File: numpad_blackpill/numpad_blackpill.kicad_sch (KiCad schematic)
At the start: 51 parts

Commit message: working on numpad PCB
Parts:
- removed U?: STM32F411CEUx, Package_DFN_QFN:QFN-48-1EP_7x7mm_P0.5mm_EP5.6x5.6mm, symbol MCU_ST_STM32F4:STM32F411CEUx
- added U1: YAAJ_BlackPill, Kicad-STM32-master:YAAJ_BlackPill_SWD_1, symbol YAAJ_BlackPill:YAAJ_BlackPill
- SW1, SW10, SW11, SW12, SW13, SW14, SW15, SW16, SW17, SW18, SW19, SW2, SW20, SW21, SW22, SW23, SW24, SW25, SW3, SW4, SW5, SW6, SW7, SW8, SW9: renamed from SW?; footprint (none) -> Button_Switch_Keyboard:SW_Cherry_MX_1.00u_PCB
- gave numbers to parts that had none: 25
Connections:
- net Col1: now also U1.13 (PB5)
- net Col2: now also U1.14 (PB6)
- net Col3: now also U1.15 (PB7)
- net Col4: now also U1.19 (PB8)
- net Col5: now also U1.20 (PB9)
- net Reset: now also U1.22 (RST)
- net Row1: now also U1.24 (PA1)
- net Row2: now also U1.25 (PA2)
- net Row3: now also U1.26 (PA3)
- net Row4: now also U1.27 (PA4)
- net Row5: now also U1.28 (PA5)

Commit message: finished basic numpad with blackpill
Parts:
- removed D1, D15, D22, D24, D6: 1N4148, Diode_THT:D_DO-35_SOD27_P7.62mm_Horizontal, symbol Diode:1N4148
- removed SW1, SW15, SW22, SW24, SW6: SW_Push, Button_Switch_Keyboard:SW_Cherry_MX_1.00u_PCB, symbol Switch:SW_Push
- removed U1: YAAJ_BlackPill, Kicad-STM32-master:YAAJ_BlackPill_SWD_1, symbol YAAJ_BlackPill:YAAJ_BlackPill
- added U1: YAAJ_BlackPill_Part_Like_SWD_Breakout, Kicad-STM32-master:YAAJ_BlackPill_SWD_3, symbol YAAJ_BlackPill_Part_Like_SWD_Breakout:YAAJ_BlackPill_Part_Like_SWD_Breakout
- SW19: renamed from SW23; footprint Button_Switch_Keyboard:SW_Cherry_MX_1.00u_PCB -> Button_Switch_Keyboard:SW_Cherry_MX_2.00u_Vertical_PCB
- SW20: renamed from SW25; footprint Button_Switch_Keyboard:SW_Cherry_MX_1.00u_PCB -> Button_Switch_Keyboard:SW_Cherry_MX_2.00u_Vertical_PCB
- SW8: renamed from SW10; footprint Button_Switch_Keyboard:SW_Cherry_MX_1.00u_PCB -> Button_Switch_Keyboard:SW_Cherry_MX_2.00u_PCB
- renumbered D2 to D1, D12 to D10, D13 to D11, D14 to D12, D16 to D13, D17 to D14, D18 to D15, D19 to D16, D20 to D17, D21 to D18, D23 to D19, D3 to D2, D25 to D20, D4 to D3, D5 to D4, D7 to D5, D8 to D6, D9 to D7, D10 to D8, D11 to D9, SW2 to SW1, SW12 to SW10, SW13 to SW11, SW14 to SW12, SW16 to SW13, SW17 to SW14, SW18 to SW15, SW19 to SW16, SW20 to SW17, SW21 to SW18, SW3 to SW2, SW4 to SW3, SW5 to SW4, SW7 to SW5, SW8 to SW6, SW9 to SW7, SW11 to SW9
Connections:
- net Col1: now also U1.7 (PA10)
- net Col2: now also U1.6 (PA9)
- net Col3: now also U1.13 (PB5)
- net Col4: now also U1.14 (PB6)
- net Col5: now also U1.15 (PB7)
- net Reset: now also U1.22 (RST)
- net Row1: now also U1.28 (PA5)
- net Row2: now also U1.27 (PA4)
- net Row3: now also U1.26 (PA3)
- net Row4: now also U1.25 (PA2)
- net Row5: now also U1.24 (PA1)
- new net GND: U1.17 (GND), U1.18 (GND)
- no-connect marks 0 -> 20

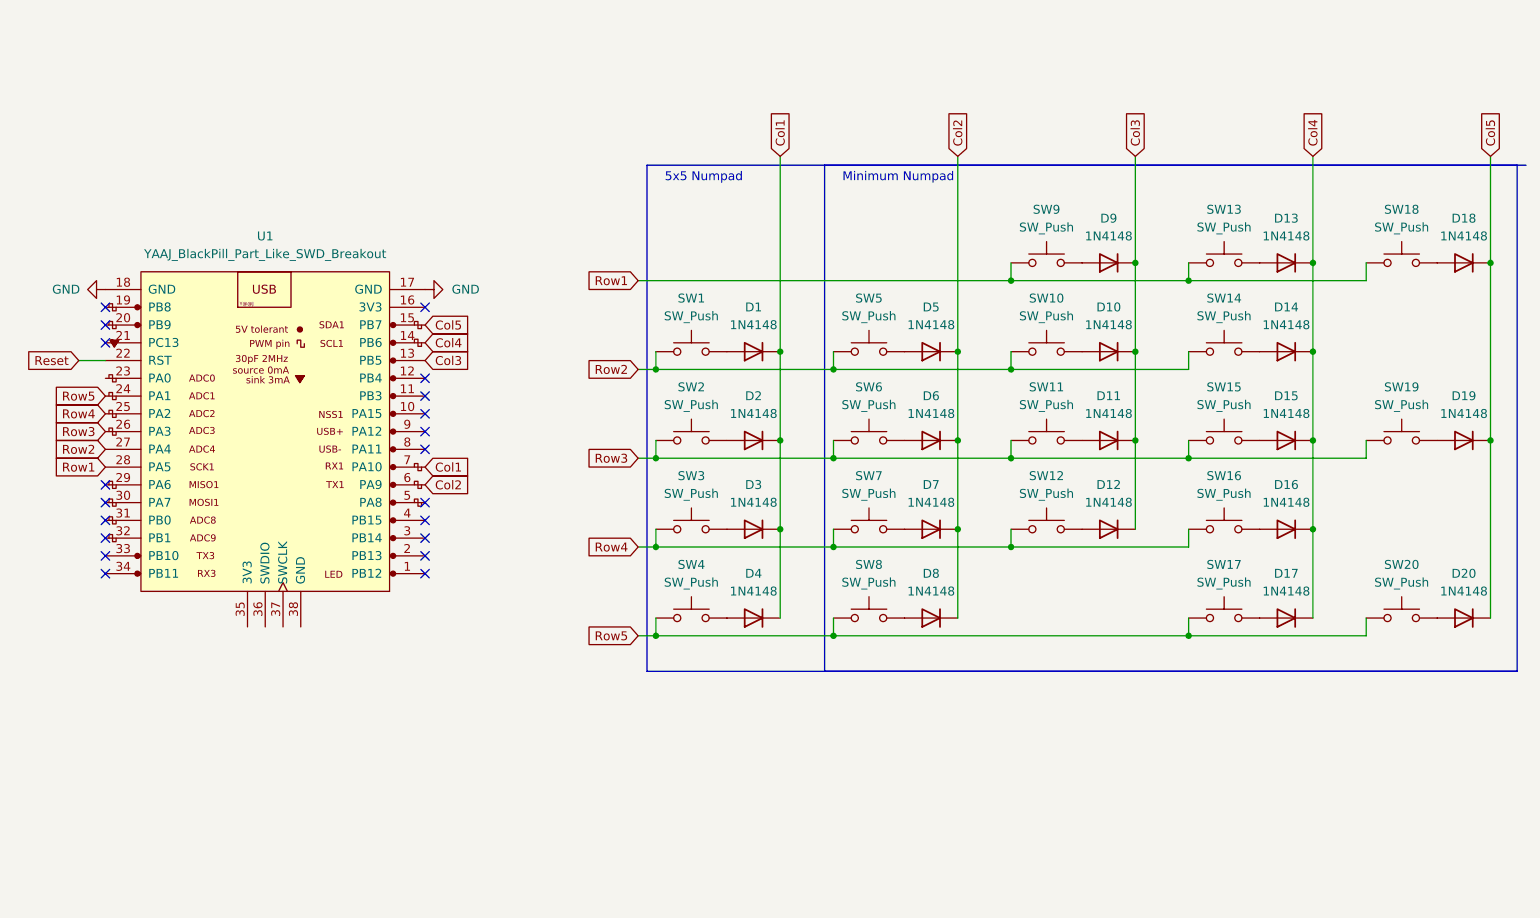
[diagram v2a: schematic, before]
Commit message: removed encoder from numpad
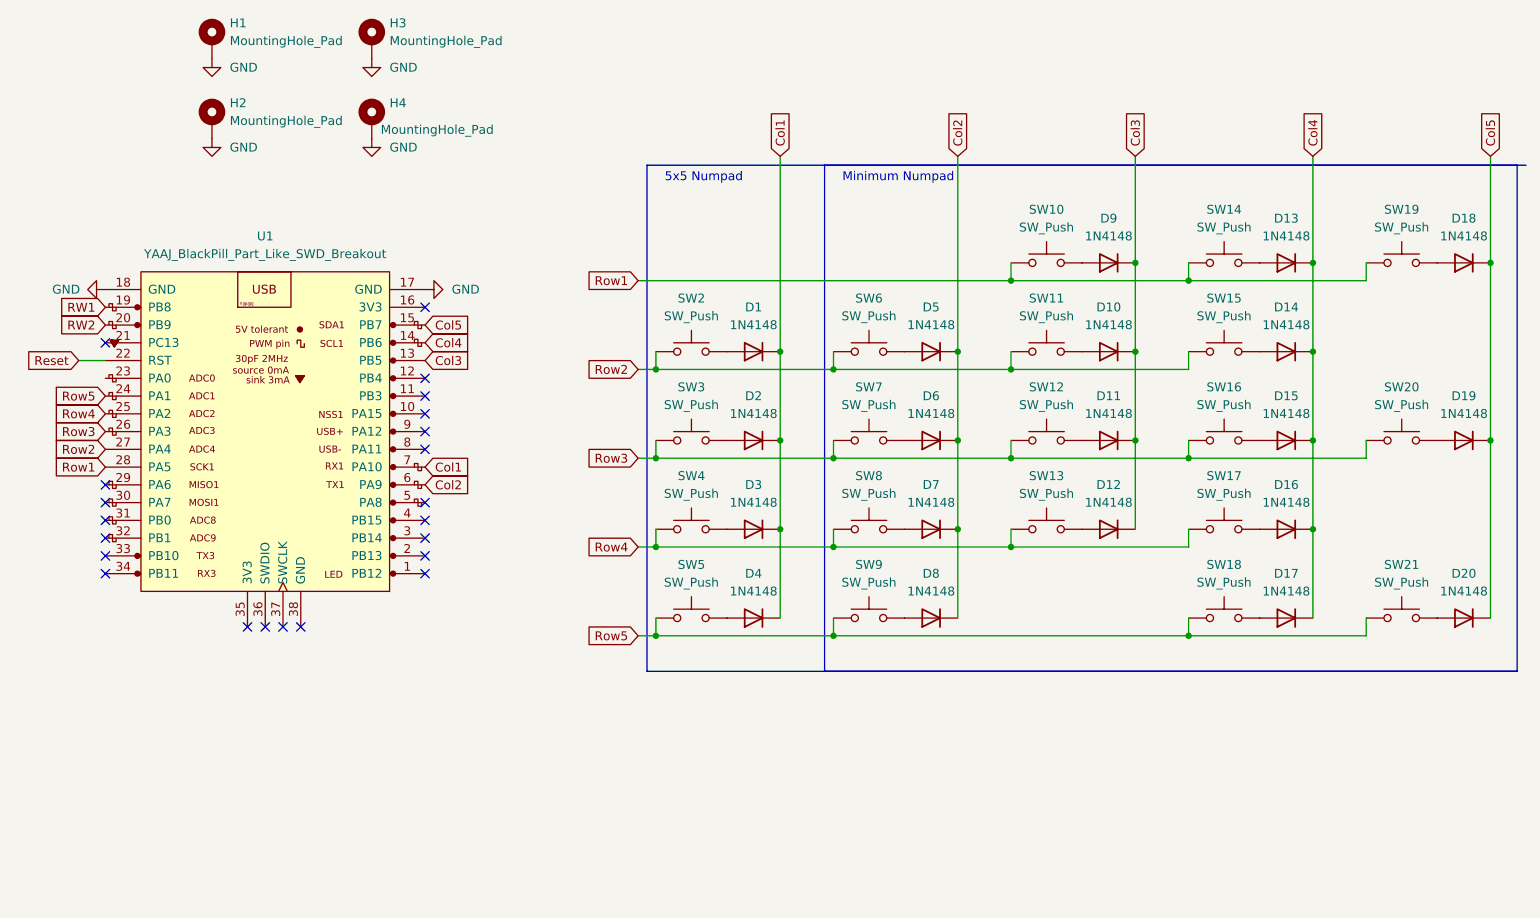
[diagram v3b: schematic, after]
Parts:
- added H1, H2, H3, H4: MountingHole_Pad, MountingHole:MountingHole_2mm, symbol Mechanical:MountingHole_Pad
- renumbered SW9 to SW10, SW10 to SW11, SW11 to SW12, SW12 to SW13, SW13 to SW14, SW14 to SW15, SW15 to SW16, SW16 to SW17, SW17 to SW18, SW18 to SW19, SW1 to SW2, SW19 to SW20, SW20 to SW21, SW2 to SW3, SW3 to SW4, SW4 to SW5, SW5 to SW6, SW6 to SW7, SW7 to SW8, SW8 to SW9
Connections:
- net GND: now also H1.1, H2.1, H3.1, H4.1
- net RW1: now reaches U1.19 (PB8)
- net RW2: now reaches U1.20 (PB9)
- no-connect marks 20 -> 22
